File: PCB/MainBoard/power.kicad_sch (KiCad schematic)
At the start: 50 parts, among them J1 Conn_01x01_Female, J17 Conn_01x02_Socket, J2 Conn_01x01_Female, J3 Conn_01x01_Female, J4 Conn_01x01_Pin, U1 TPS56339DDC, U2 TPS56339DDC, U5 TPS56339DDC

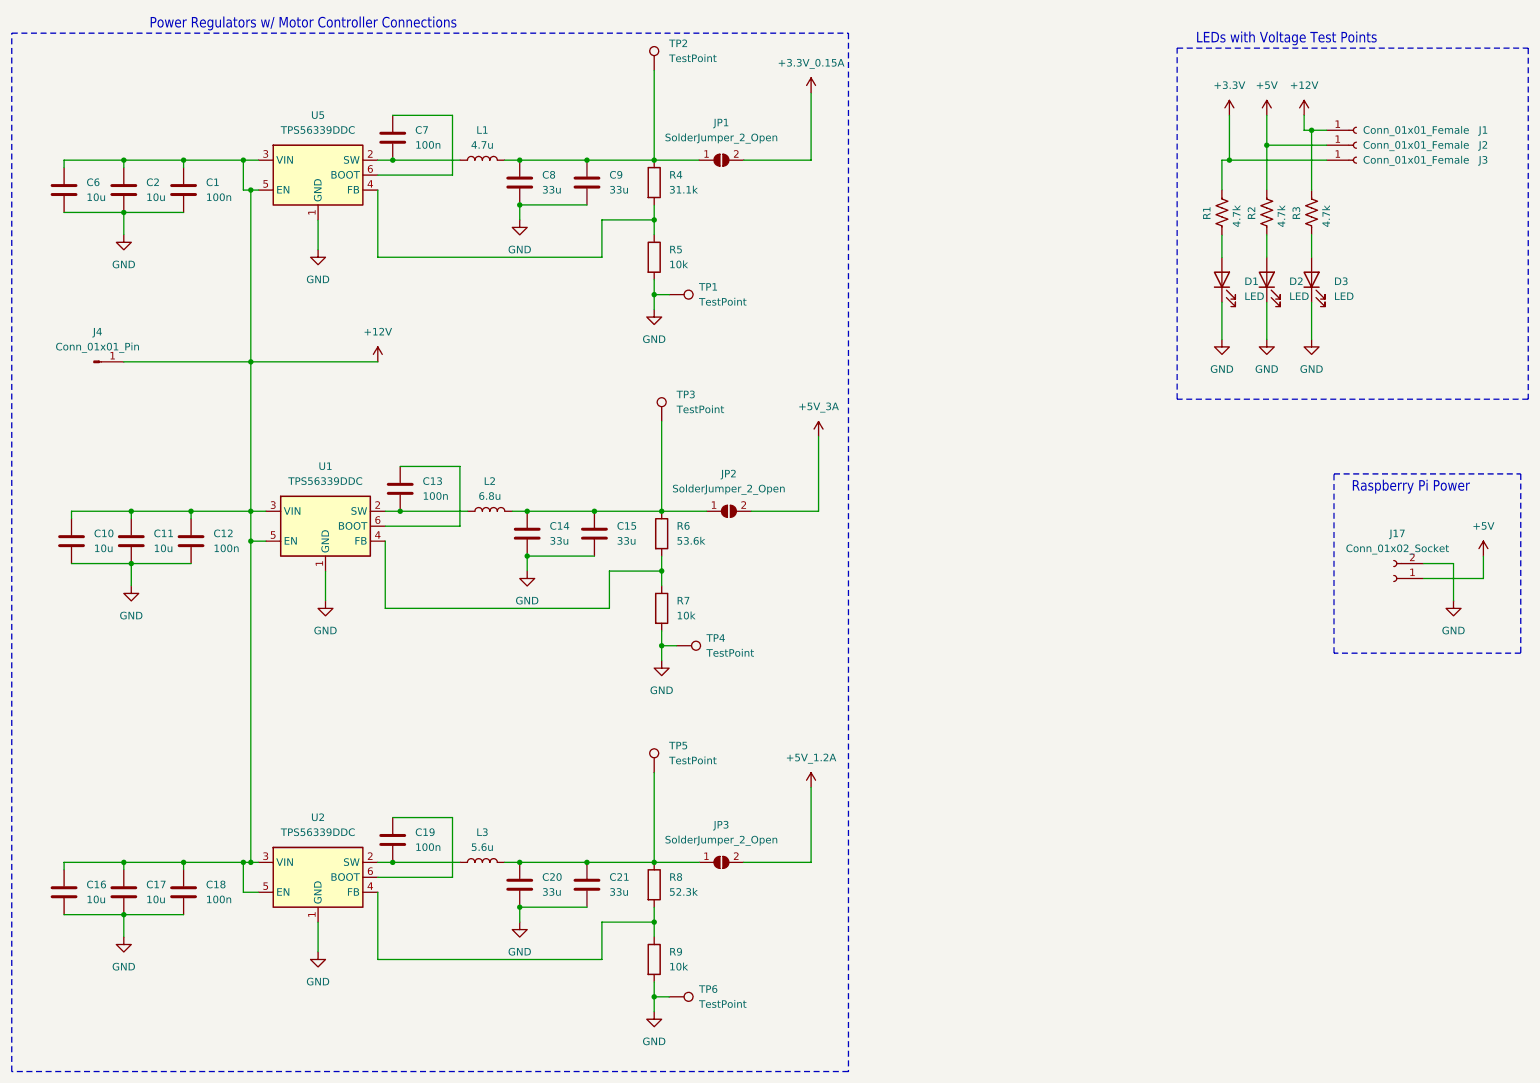
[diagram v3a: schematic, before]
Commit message: updating power schematics, and power lines
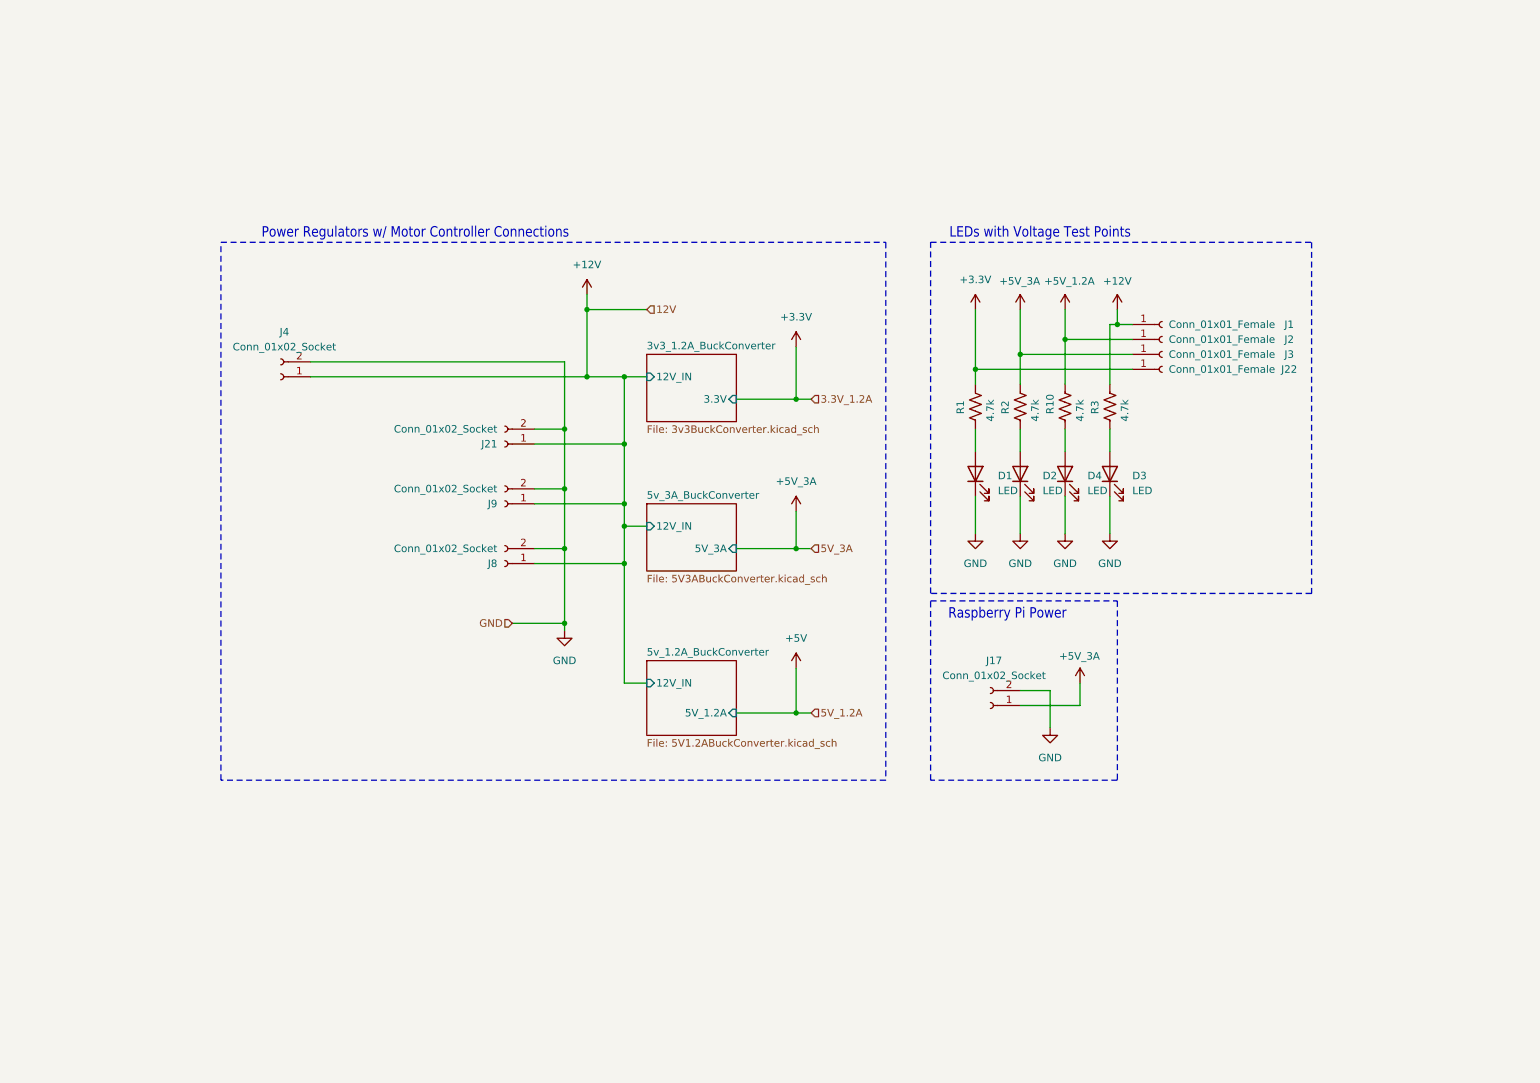
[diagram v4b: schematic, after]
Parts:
- removed C1, C12, C13, C18, C19, C7: 100n, symbol Device:C
- removed C10, C11, C16, C17, C2, C6: 10u, symbol Device:C
- removed C14, C15, C20, C21, C8, C9: 33u, symbol Device:C
- removed J4: Conn_01x01_Pin, symbol Connector:Conn_01x01_Pin
- removed JP1, JP2, JP3: SolderJumper_2_Open, symbol Jumper:SolderJumper_2_Open
- removed L1: 4.7u, symbol Device:L
- removed L2: 6.8u, symbol Device:L
- removed L3: 5.6u, symbol Device:L
- removed R4: 31.1k, symbol Device:R
- removed R5, R7, R9: 10k, symbol Device:R
- removed R6: 53.6k, symbol Device:R
- removed R8: 52.3k, symbol Device:R
- removed TP1, TP2, TP3, TP4, TP5, TP6: TestPoint, symbol Connector:TestPoint
- removed U1, U2, U5: TPS56339DDC, Package_TO_SOT_SMD:SOT-23-6, symbol Regulator_Switching:TPS56339DDC
- added D4: LED, LED_THT:LED_D3.0mm_Clear, symbol Device:LED
- added J21, J4, J8, J9: Conn_01x02_Socket, symbol Connector:Conn_01x02_Socket
- added J22: Conn_01x01_Female, Connector_PinHeader_1.00mm:PinHeader_1x01_P1.00mm_Vertical, symbol Connector:Conn_01x01_Female
- added R10: 4.7k, Resistor_THT:R_Axial_DIN0207_L6.3mm_D2.5mm_P7.62mm_Horizontal, symbol Device:R_US
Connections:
- net +12V: now also J21.1 (Pin_1), J4.1 (Pin_1), J8.1 (Pin_1), J9.1 (Pin_1)
- net +3.3V: now also J22.1 (Pin_1); no longer J3.1 (Pin_1)
- net +5V: no longer J17.1 (Pin_1), J2.1 (Pin_1), R2.1
- net +5V_1.2A: now also J2.1 (Pin_1), R10.1
- net +5V_3A: now also J17.1 (Pin_1), J3.1 (Pin_1), R2.1
- net GND: now also D4.1 (K), J21.2 (Pin_2), J4.2 (Pin_2), J8.2 (Pin_2), J9.2 (Pin_2)
- new net: D4.2 (A), R10.2
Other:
- added sheet 3v3_1.2A_BuckConverter (3v3BuckConverter.kicad_sch)
- added sheet 5v_1.2A_BuckConverter (5V1.2ABuckConverter.kicad_sch)
- added sheet 5v_3A_BuckConverter (5V3ABuckConverter.kicad_sch)
- moved on the sheet: D1, D2, D3, J1, J17, J2, J3, R1, R2, R3

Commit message: passed ERC in schematic
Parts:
- removed J1, J2, J22, J3: Conn_01x01_Female, Connector_PinHeader_1.00mm:PinHeader_1x01_P1.00mm_Vertical, symbol Connector:Conn_01x01_Female
- added J1, J13, J2, J3: Conn_01x01_Socket, Connector_PinHeader_2.54mm:PinHeader_1x01_P2.54mm_Vertical, symbol Connector:Conn_01x01_Socket
- J17, J21, J4, J8, J9: footprint (none) -> Connector_Wire:SolderWire-0.5sqmm_1x02_P4.8mm_D0.9mm_OD2.3mm
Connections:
- net +12V: now also J1.1 (Pin_1)
- net +5V_1.2A: now also R2.1, J3.1 (Pin_1); no longer R10.1
- net +5V_3A: now also R10.1, J2.1 (Pin_1); no longer R2.1
- net +3.3V renamed +3.3V_1.2A
- net +3.3V_1.2A: now also J13.1 (Pin_1)
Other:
- sheet 3v3_1.2A_BuckConverter ports: added +12V, +3.3V_1.2A; removed 12V_IN, 3.3V
- sheet 5v_1.2A_BuckConverter ports: added +12V, +5V_1.2A; removed 12V_IN, 5V_1.2A
- sheet 5v_3A_BuckConverter ports: added +12V, +5V_3A; removed 12V_IN, 5V_3A

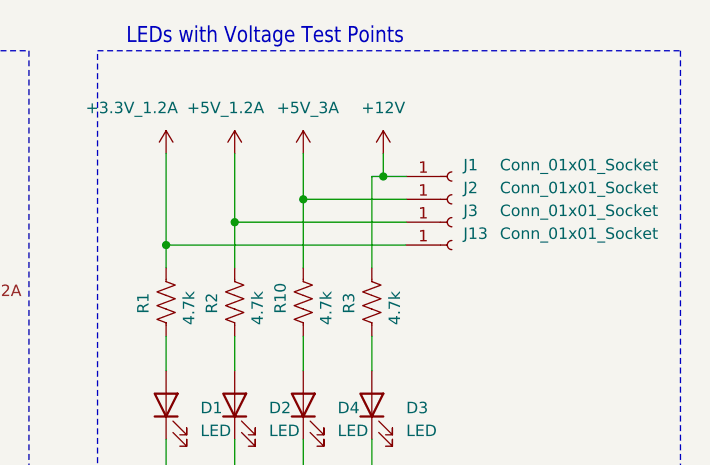
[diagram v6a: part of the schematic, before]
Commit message: final layout v1 - unconnected
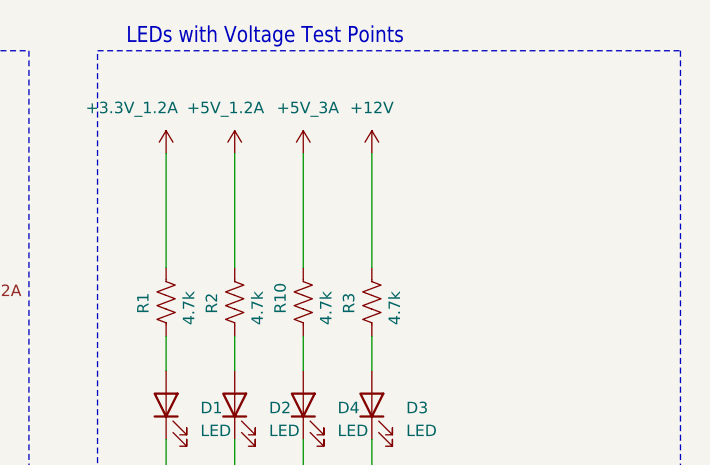
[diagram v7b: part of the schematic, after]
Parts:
- removed J1, J13, J2, J3: Conn_01x01_Socket, Connector_PinHeader_2.54mm:PinHeader_1x01_P2.54mm_Vertical, symbol Connector:Conn_01x01_Socket

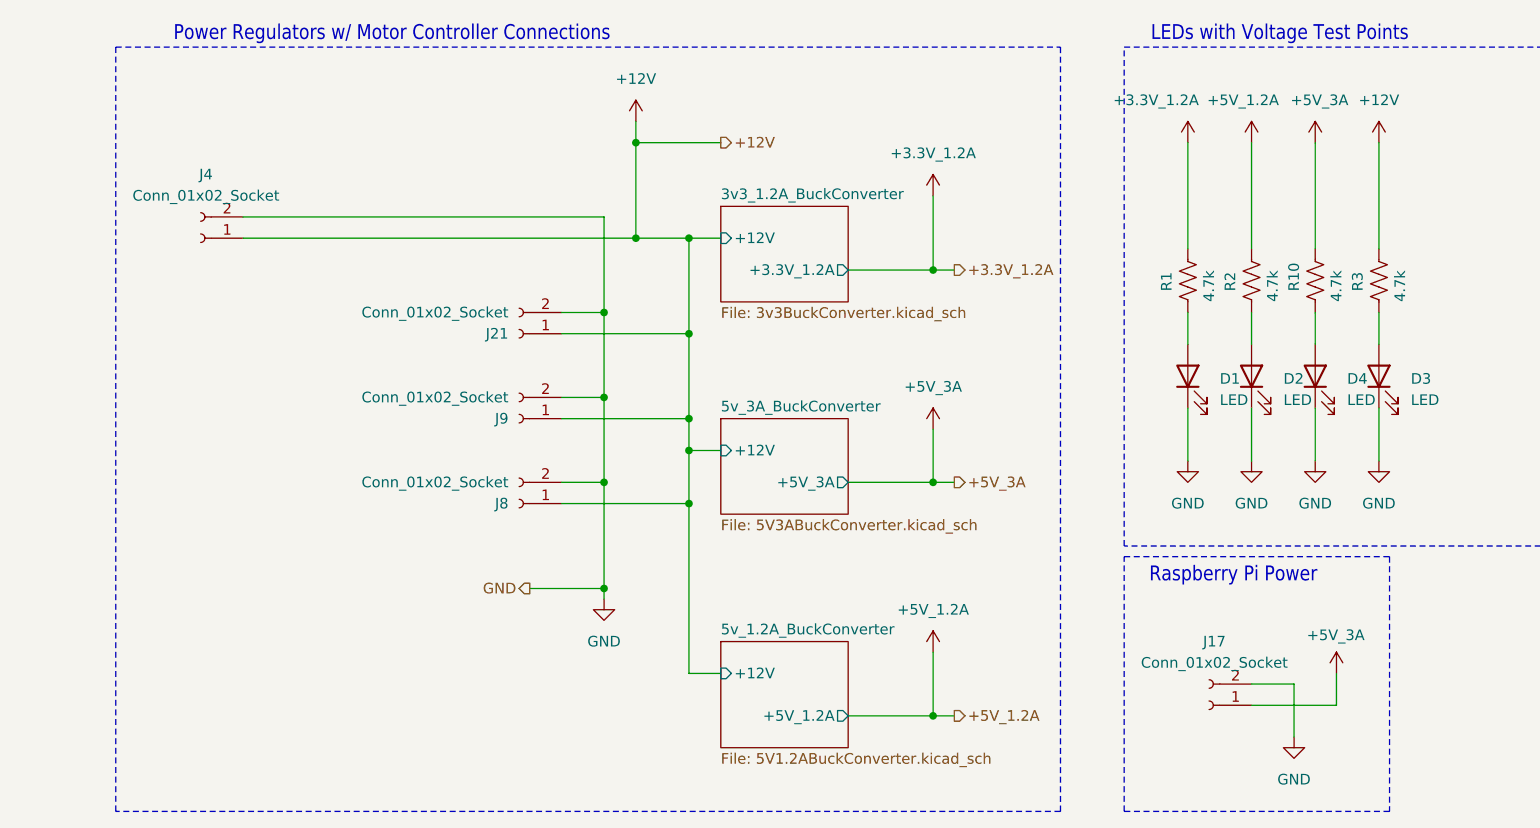
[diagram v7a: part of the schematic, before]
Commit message: updating PCB with new components and proper footprints, still need to fix footprint matching issue.
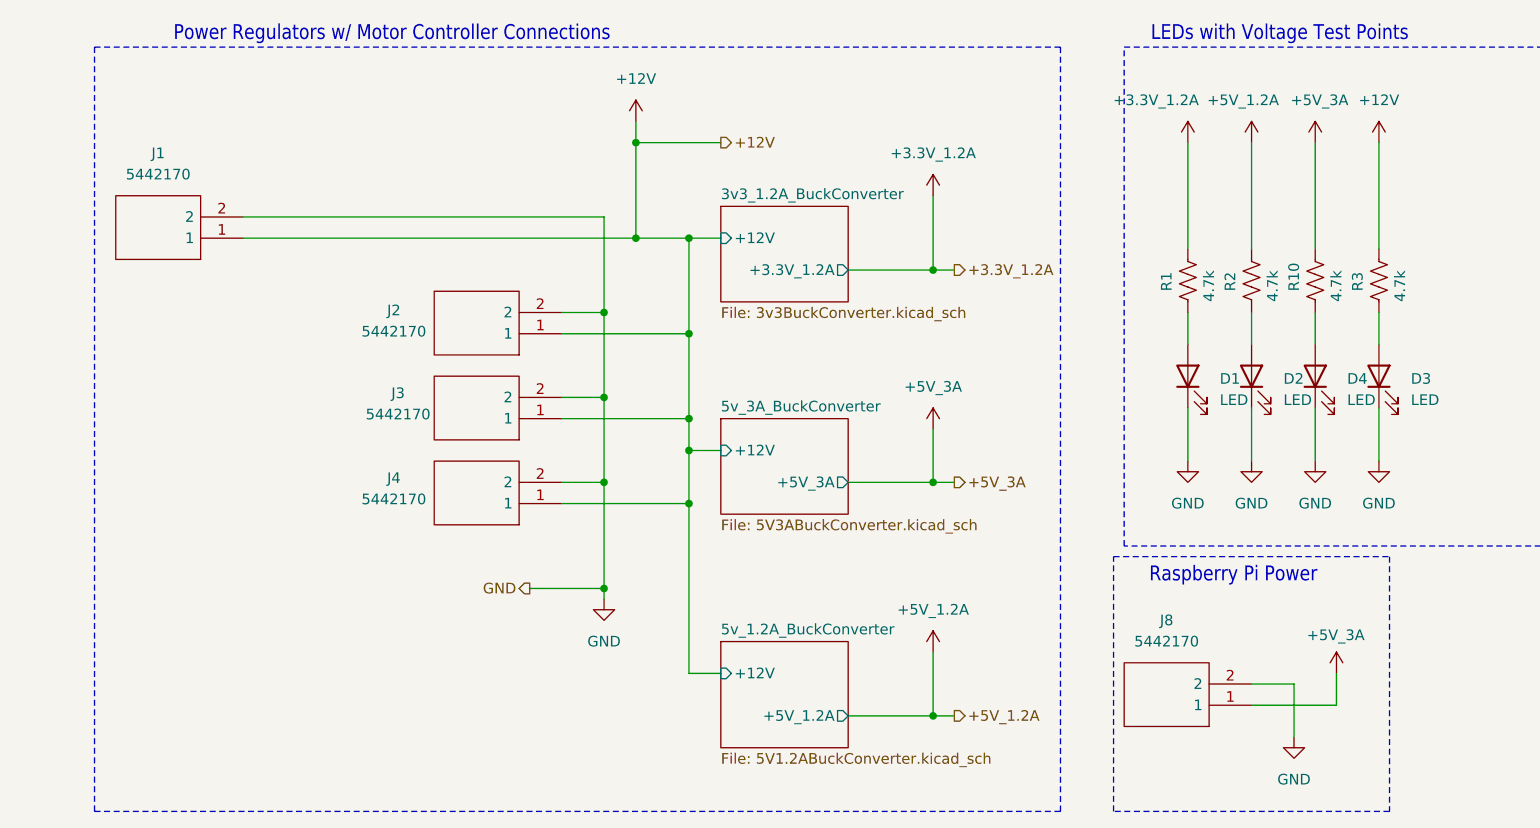
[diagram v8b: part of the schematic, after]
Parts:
- removed J17, J21, J4, J8, J9: Conn_01x02_Socket, Connector_Wire:SolderWire-0.5sqmm_1x02_P4.8mm_D0.9mm_OD2.3mm, symbol Connector:Conn_01x02_Socket
- added J1, J2, J3, J4, J8: 5442170, ProjectLibrary:5442170, symbol CustomSymbols:5442170
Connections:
- net +12V: now also J1.1, J2.1, J3.1, J4.1
- net +5V_3A: now also J8.1
- net GND: now also J1.2, J2.2, J3.2, J4.2, J8.2
